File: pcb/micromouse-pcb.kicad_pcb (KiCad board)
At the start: 4 copper layers, 100 x 114 mm, 129 parts, among them J1 JST_XH_B2B-XH-A_1x02_P2.50mm_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, J10 PinSocket_1x08_P2.54mm_Vertic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, J11 PinSocket_1x08_P2.54mm_Vertic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, J2 PinHeader_1x02_P2.54mm_Vertic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, J3 JST_XH_B3B-XH-A_1x03_P2.50mm_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, J5 JST_PH_B6B-PH-K_1x06_P2.00mm_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, J6 JST_PH_B6B-PH-K_1x06_P2.00mm_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, Q1 SOT-23, Q10 LED_D3.0mm_Clear, Q11 SOT-23, Q12 LED_D3.0mm_Clear, Q13 SOT-23, Q14 SMD phototransistor 940nm, DA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, Q15 SOT-23, Q16 SMD phototransistor 940nm, DA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, Q17 SOT-23, Q18 SMD phototransistor 940nm, DA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, Q19 SOT-23, Q2 LED_D3.0mm_Clear, Q20 SMD phototransistor 940nm, DA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, Q21 SOT-23, Q22 SMD phototransistor 940nm, DA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, Q23 SOT-23, Q24 SMD phototransistor 940nm, DA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, Q25 SOT-23, Q26 SMD phototransistor 940nm, DA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, Q27 SOT-23, Q28 SMD phototransistor 940nm, DA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, Q29 SOT-23, Q3 SOT-23, Q30 SOT-23, Q31 SOT-23, Q32 SOT-23, Q33 SOT-23, Q34 SOT-23, Q35 SOT-23, Q36 SOT-23, Q37 SOT-23, Q4 LED_D3.0mm_Clear, Q5 SOT-23, Q6 LED_D3.0mm_Clear, Q7 SOT-23, Q8 LED_D3.0mm_Clear, Q9 SOT-23, SW1 SW_PUSH_6mm, U1 TSOT-23-6, U4 SOIC-24W_7.5x15.4mm_P1.27mm, U5 SOIC-24W_7.5x15.4mm_P1.27mm

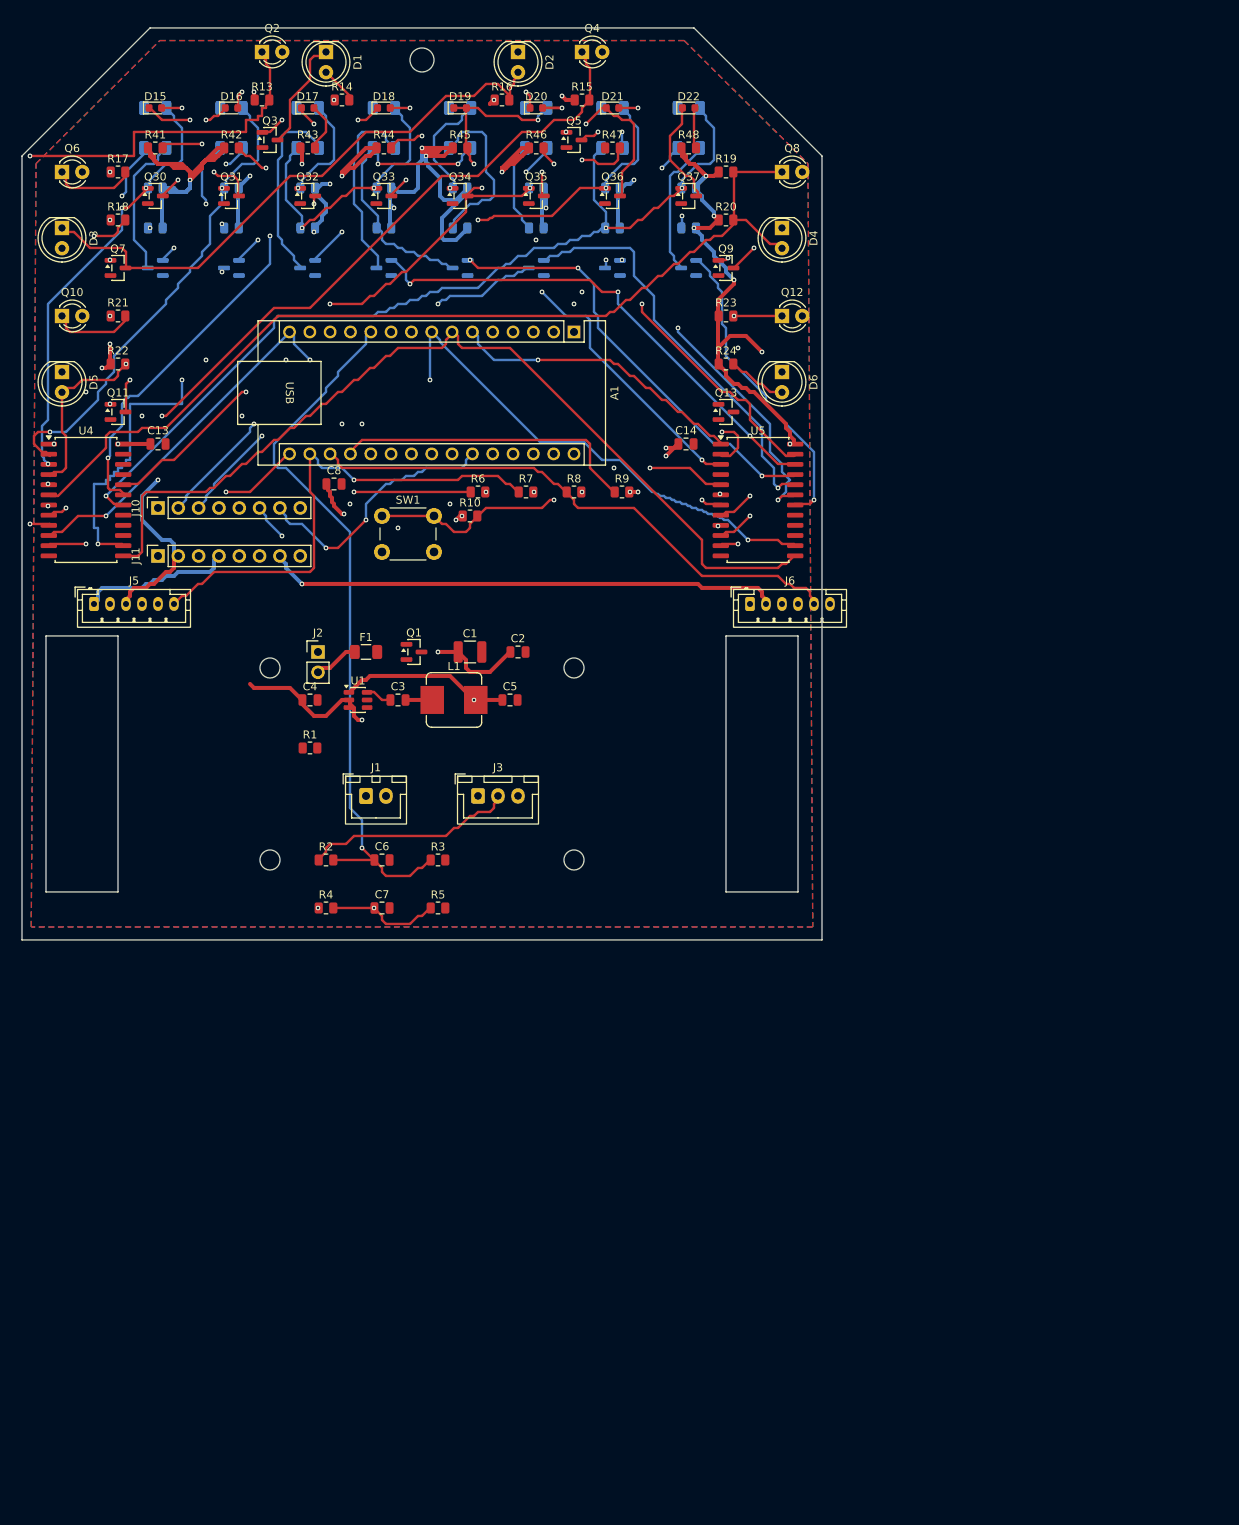
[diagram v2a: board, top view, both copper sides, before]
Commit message: Rev 4: WROOM-1 module, 1S power, direct wall ADC, pro routing
User requests: mux only for line array (walls direct to ADC), exact ESP32
library footprint+3D, exact N20 library, speed+RTOS, 1S LiPo, 3 user
buttons, rear USB-C, JTAG outlet, wall indicator LEDs, professional routing.

- ESP32-S3-WROOM-1 (SMD, stock footprint + 3D STEP), antenna overhanging
  the right edge per Espressif rules (interior placement disallowed).
  Locked pin map adversarially verified: JTAG on the real quad IO39-42,
  ENC2 on UART0 pins with 1k boot-contention guards (review blocker),
  straps as idle-low outputs with pull-downs, buttons IO0/35/36.
- 1S LiPo: TPS63001 buck-boost (buck can't hold 3.3V from a sagging cell),
  no balance lead, divider rescaled 4.2V->2.52V (ADC calibrated-range
  review fix), motors on raw cell (3V-wound N20s).
- Sensors: walls direct on ADC1 IO1-6 (fired pair sampled in parallel),
  line array on one CD74HC4067 (HC swap: HEF4067 out of spec at 3.3V),
  emitters ganged in 4 groups (U5 deleted), 6 PMOS wall indicators
  (LED ON = wall seen) + 8 line indicators on top.
- Project-local N20 library (footprint + hand-authored VRML from Pololu
  drawing 0J949); motors placed true-size, keep-outs match real 33mm body.
- Router upgrades: string-pulling post-pass (canonical diagonal+straight
  45-degree geometry, clearance-verified per candidate -- segment count
  halved), two power-width tiers (0.35mm for the SON-pad nets), padded
  slot/hole keep-outs, via-radius-aware keepout test.
- Fixed a real generator bug: loop Z-bend wires shorted nets every 6th
  sensor (netlist audit caught D3/D9 anodes folded into cathode nets) --
  all loop wiring is now straight by construction.

100x114mm, 4 layers, 152 footprints, 1077 tracks / 167 vias, ERC 0,
DRC 0 errors; 12 connections left for GUI finishing (JTAG fan-out, one
USB pair, buck-boost hookup) -- listed in PROJECT_NOTES.

Co-Authored-By: Claude Fable 5 <noreply@anthropic.com>
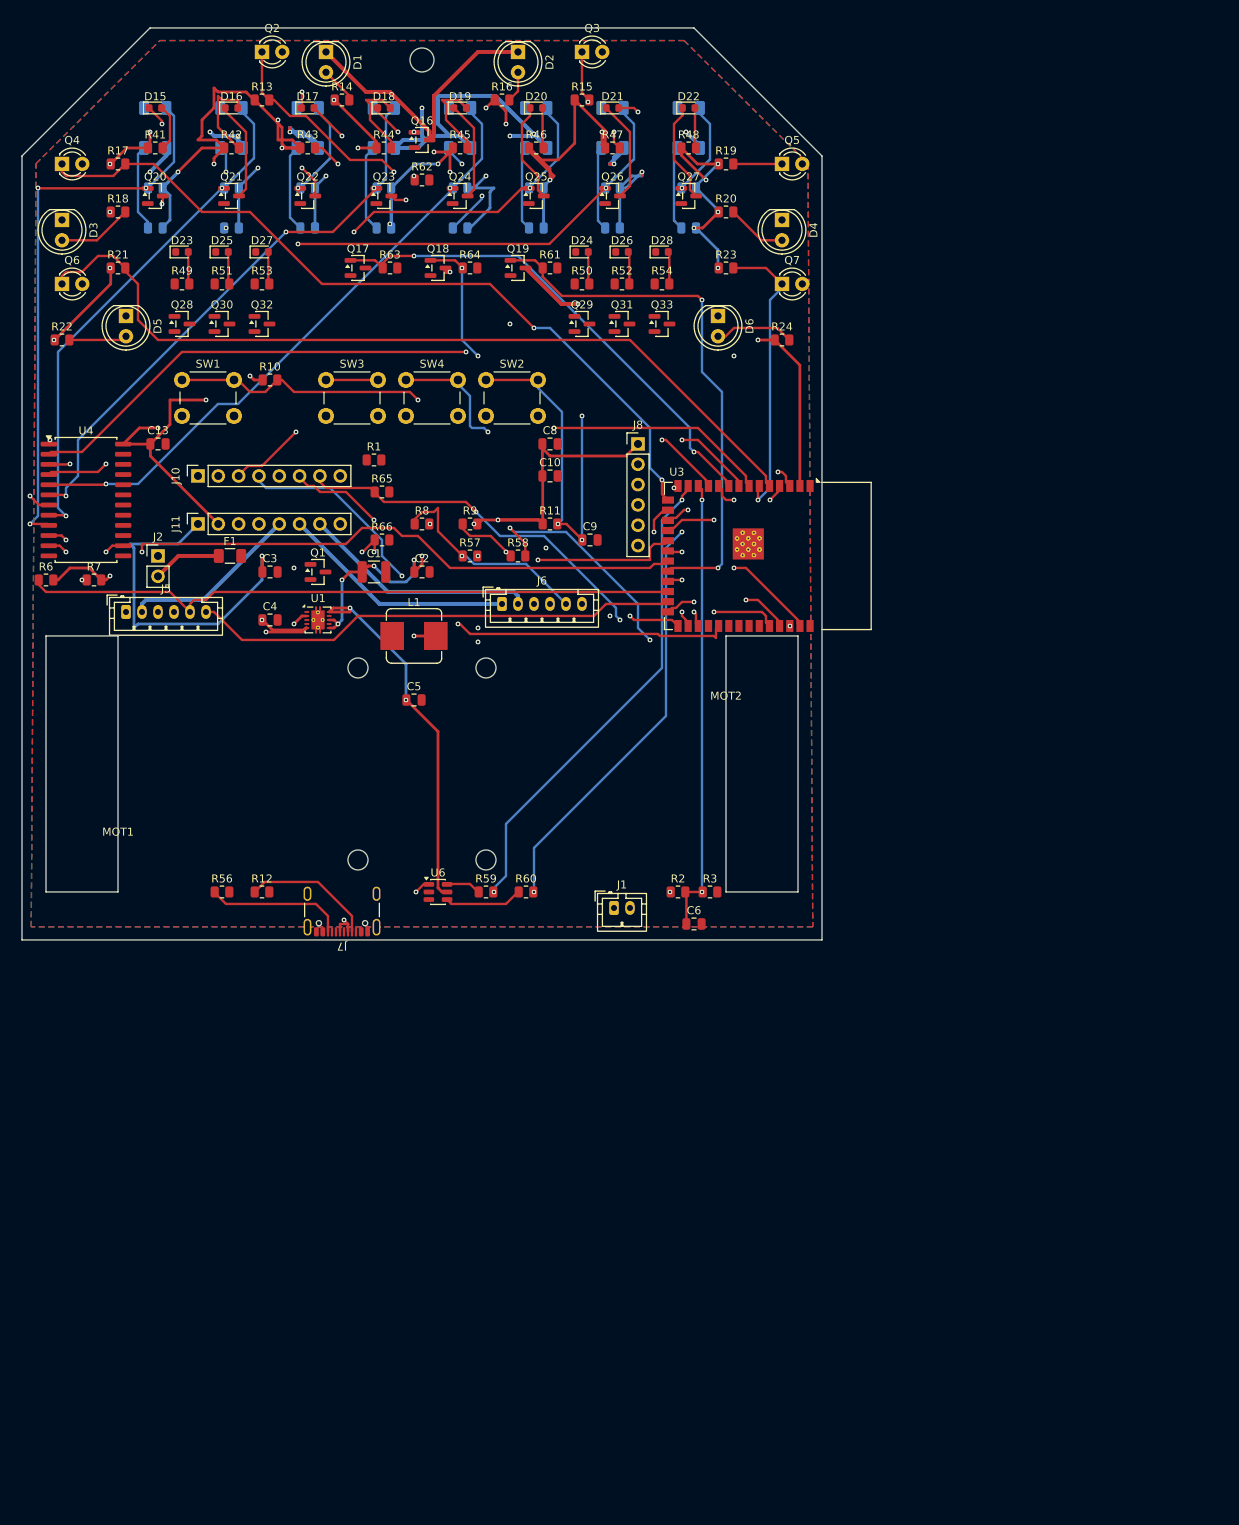
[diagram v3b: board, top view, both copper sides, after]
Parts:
- removed A1: Arduino_Nano, Arduino_Nano
- removed C14, C7: C_0805_2012Metric, C_0805_2012Metric
- removed J3: JST_XH_B3B-XH-A_1x03_P2.50mm_Vertical, JST_XH_B3B-XH-A_1x03_P2.50mm_Vertical
- removed Q34, Q35, Q36, Q37: SOT-23, SOT-23
- removed R4, R5: R_0805_2012Metric, R_0805_2012Metric
- removed U5: SOIC-24W_7.5x15.4mm_P1.27mm, SOIC-24W_7.5x15.4mm_P1.27mm
- added C10: C_0805_2012Metric, C_0805_2012Metric, F.Cu at (66.0, 56.0)
- added C9: C_0805_2012Metric, C_0805_2012Metric, F.Cu at (71.0, 64.0)
- added D23: LED_0603_1608Metric, LED_0603_1608Metric, F.Cu at (20.0, 28.0)
- added D24: LED_0603_1608Metric, LED_0603_1608Metric, F.Cu at (70.0, 28.0)
- added D25: LED_0603_1608Metric, LED_0603_1608Metric, F.Cu at (25.0, 28.0)
- added D26: LED_0603_1608Metric, LED_0603_1608Metric, F.Cu at (75.0, 28.0)
- added D27: LED_0603_1608Metric, LED_0603_1608Metric, F.Cu at (30.0, 28.0)
- added D28: LED_0603_1608Metric, LED_0603_1608Metric, F.Cu at (80.0, 28.0)
- added J7: USB_C_Receptacle_GCT_USB4105-xx-A_16P_TopMnt_Horizontal, USB_C_Receptacle_GCT_USB4105-xx-A_16P_TopMnt_Horizontal, F.Cu at (40.0, 109.3)
- added J8: PinHeader_1x06_P2.54mm_Vertical, PinHeader_1x06_P2.54mm_Vertical, F.Cu at (77.0, 52.0)
- added MOT1: N20_Motor_Encoder, N20_Motor_Encoder, F.Cu at (12.0, 92.0)
- added MOT2: N20_Motor_Encoder, N20_Motor_Encoder, F.Cu at (88.0, 92.0)
- added R11: R_0805_2012Metric, R_0805_2012Metric, F.Cu at (66.0, 62.0)
- added R12: R_0805_2012Metric, R_0805_2012Metric, F.Cu at (30.0, 108.0)
- added R49: R_0805_2012Metric, R_0805_2012Metric, F.Cu at (20.0, 32.0)
- added R50: R_0805_2012Metric, R_0805_2012Metric, F.Cu at (70.0, 32.0)
- added R51: R_0805_2012Metric, R_0805_2012Metric, F.Cu at (25.0, 32.0)
- added R52: R_0805_2012Metric, R_0805_2012Metric, F.Cu at (75.0, 32.0)
- added R53: R_0805_2012Metric, R_0805_2012Metric, F.Cu at (30.0, 32.0)
- added R54: R_0805_2012Metric, R_0805_2012Metric, F.Cu at (80.0, 32.0)
- added R56: R_0805_2012Metric, R_0805_2012Metric, F.Cu at (25.0, 108.0)
- added R57: R_0805_2012Metric, R_0805_2012Metric, F.Cu at (56.0, 66.0)
- added R58: R_0805_2012Metric, R_0805_2012Metric, F.Cu at (62.0, 66.0)
- added R59: R_0805_2012Metric, R_0805_2012Metric, F.Cu at (58.0, 108.0)
- added R60: R_0805_2012Metric, R_0805_2012Metric, F.Cu at (63.0, 108.0)
- added R61: R_0805_2012Metric, R_0805_2012Metric, F.Cu at (66.0, 30.0)
- added R62: R_0805_2012Metric, R_0805_2012Metric, F.Cu at (50.0, 19.0)
- added R63: R_0805_2012Metric, R_0805_2012Metric, F.Cu at (46.0, 30.0)
- added R64: R_0805_2012Metric, R_0805_2012Metric, F.Cu at (56.0, 30.0)
- added R65: R_0805_2012Metric, R_0805_2012Metric, F.Cu at (45.0, 58.0)
- added R66: R_0805_2012Metric, R_0805_2012Metric, F.Cu at (45.0, 64.0)
- added SW2: SW_PUSH_6mm, SW_PUSH_6mm, F.Cu at (58.0, 44.0)
- added SW3: SW_PUSH_6mm, SW_PUSH_6mm, F.Cu at (38.0, 44.0)
- added SW4: SW_PUSH_6mm, SW_PUSH_6mm, F.Cu at (48.0, 44.0)
- added U3: ESP32-S3-WROOM-1, ESP32-S3-WROOM-1, F.Cu at (93.2, 66.0)
- added U6: SOT-23-6, SOT-23-6, F.Cu at (52.0, 108.0)
- D15, D16, D17, D18, D19, D20, D21, D22: value Indicator LED 0603 super-red AlInGaP, high-efficiency bin REQUIRED at 1.4mA (e.g. Kingbright APT1608SURCK; LD271 base s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 -> LED_0603_1608Metric
- J1: value JST_XH_B2B-XH-A_1x02_P2.50mm_Vertical -> JST_PH_B2B-PH-K_1x02_P2.00mm_Vertical; footprint JST_XH_B2B-XH-A_1x02_P2.50mm_Vertical -> JST_PH_B2B-PH-K_1x02_P2.00mm_Vertical
- L1: value 3.3uH -> 1.5uH
- Q10, Q12, Q8: value LED_D3.0mm_Clear -> LED_1206_3216Metric; footprint LED_D3.0mm_Clear -> LED_1206_3216Metric; moved to B.Cu
- Q11, Q13, Q9: value SOT-23 -> LED_1206_3216Metric; footprint SOT-23 -> LED_1206_3216Metric; moved to B.Cu
- Q14: value SMD phototransistor 940nm, DAYLIGHT-FILTERED REQUIRED (e.g. Osram SFH320FA -- an unfiltered part re-opens optical feedb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 -> LED_1206_3216Metric
- Q15: value SOT-23 -> LED_1206_3216Metric; footprint SOT-23 -> LED_1206_3216Metric
- Q16, Q18, Q20, Q22, Q24, Q26, Q28: value SMD phototransistor 940nm, DAYLIGHT-FILTERED REQUIRED (e.g. Osram SFH320FA -- an unfiltered part re-opens optical feedb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 -> SOT-23; footprint LED_1206_3216Metric -> SOT-23; moved to F.Cu
- Q17, Q19, Q21, Q23, Q25, Q27, Q29: moved to F.Cu
- Q3, Q5, Q7: value SOT-23 -> LED_D3.0mm_Clear; footprint SOT-23 -> LED_D3.0mm_Clear
- R26, R28, R30, R32, R34, R36, R38, R40: value 120 -> R_0805_2012Metric
- U1: value TSOT-23-6 -> Texas_DRC0010J_ThermalVias; footprint TSOT-23-6 -> Texas_DRC0010J_ThermalVias
- moved Q7 83.0 mm to (95.0, 32.0)
- moved Q8 78.7 mm to (16.7, 10.0), turned to 180 degrees
- moved Q15 69.6 mm to (83.3, 10.0)
- moved Q28 68.9 mm to (20.0, 37.0), turned to 0 degrees
- moved Q4 66.5 mm to (5.00, 17.0)
- moved Q9 65.0 mm to (26.2, 10.0), turned to 180 degrees
- moved Q14 57.1 mm to (73.8, 10.0)
- moved R6 55.1 mm to (3.00, 69.0)
- moved R7 55.1 mm to (9.00, 69.0)
- moved Q31 51.4 mm to (75.0, 37.0)
- moved Q11 50.5 mm to (45.2, 10.0), turned to 180 degrees
- moved Q12 47.9 mm to (54.8, 10.0), turned to 180 degrees
- moved Q13 44.8 mm to (64.3, 10.0), turned to 180 degrees
- moved R2 44.2 mm to (82.0, 108.0)
- moved Q3 40.5 mm to (70.0, 3.00)
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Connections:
- net VBAT_CELL1_SENSE renamed VBAT_SENSE
- C3 pad 1: Net-(U1-BST) -> VM_BATT
- C3 pad 2: Net-(U1-SW) -> GND
- D1 pad 1: Net-(D1-K) -> EMIT_FRONT_K
- D10 pad 1: Net-(D10-K) -> EMIT_LINE_K
- D11 pad 1: Net-(D10-A) -> EMIT_LINE_K
- D12 pad 1: Net-(D12-K) -> EMIT_LINE_K
- D13 pad 1: Net-(D13-K) -> EMIT_LINE_K
- D13 pad 2: LINE8_SENSE -> Net-(D13-A)
- D14 pad 1: Net-(D14-K) -> EMIT_LINE_K
- D19 pad 1: LINE6_SENSE -> Net-(D19-K)
- D19 pad 2: LINE6_SENSE -> Net-(D19-A)
- D2 pad 1: Net-(D2-K) -> EMIT_FRONT_K
- D21 pad 1: Net-(D20-A) -> Net-(D21-K)
- D3 pad 1: Net-(D2-A) -> EMIT_DIAG_K
- D4 pad 1: Net-(D4-K) -> EMIT_DIAG_K
- D4 pad 2: WALL4_SENSE -> Net-(D4-A)
- D5 pad 1: Net-(D5-K) -> EMIT_SIDE_K
- D5 pad 2: WALL6_SENSE -> Net-(D5-A)
- D6 pad 1: Net-(D6-K) -> EMIT_SIDE_K
- D7 pad 1: Net-(D7-K) -> EMIT_LINE_K
- D8 pad 1: Net-(D8-K) -> EMIT_LINE_K
- D9 pad 1: Net-(D9-K) -> EMIT_LINE_K
- D9 pad 2: LINE4_SENSE -> Net-(D9-A)
- L1 pad 1: Net-(U1-SW) -> Net-(U1-L1)
- L1 pad 2: PLUS3V3 -> Net-(U1-L2)
- Q10 pad 1: WALL5_SENSE -> LINE3_SENSE
- Q11 pad 1: WALL5_LED -> LINE4_SENSE
- Q12 pad 1: WALL6_SENSE -> LINE5_SENSE
- Q13 pad 1: WALL6_LED -> LINE6_SENSE
- Q14 pad 1: LINE1_SENSE -> LINE7_SENSE
- Q15 pad 1: LINE1_LED -> LINE8_SENSE
- Q16 pad 1: LINE2_SENSE -> WALL_EMIT_FRONT
- Q17 pad 1: LINE2_LED -> WALL_EMIT_DIAG
- Q17 pad 3: Net-(D8-K) -> EMIT_DIAG_K
- Q18 pad 1: LINE3_SENSE -> WALL_EMIT_SIDE
- Q19 pad 1: LINE3_LED -> LINE_EMIT
- Q19 pad 3: Net-(D9-K) -> EMIT_LINE_K
- Q20 pad 1: LINE4_SENSE -> LINE1_SENSE
- Q21 pad 1: LINE4_LED -> LINE2_SENSE
- Q21 pad 3: Net-(D10-K) -> Net-(D16-K)
- Q22 pad 1: LINE5_SENSE -> LINE3_SENSE
- Q23 pad 1: LINE5_LED -> LINE4_SENSE
- Q23 pad 3: Net-(D10-A) -> Net-(D18-K)
- Q24 pad 1: LINE6_SENSE -> LINE5_SENSE
- Q25 pad 1: LINE6_LED -> LINE6_SENSE
- Q25 pad 3: Net-(D12-K) -> Net-(D20-K)
- Q27 pad 1: LINE7_LED -> LINE8_SENSE
- Q27 pad 3: Net-(D13-K) -> Net-(D22-K)
- Q28 pad 1: LINE8_SENSE -> (no net)
- Q28 pad 2: GND -> (no net)
- Q29 pad 1: LINE8_LED -> (no net)
- Q29 pad 2: GND -> (no net)
- Q29 pad 3: Net-(D14-K) -> (no net)
- Q3 pad 1: WALL1_LED -> WALL2_SENSE
- Q30 pad 1: LINE1_SENSE -> (no net)
- Q30 pad 2: GND -> (no net)
- Q30 pad 3: Net-(D15-K) -> (no net)
- Q31 pad 1: LINE2_SENSE -> (no net)
- Q31 pad 2: GND -> (no net)
- Q31 pad 3: Net-(D16-K) -> (no net)
- Q32 pad 1: LINE3_SENSE -> (no net)
- Q32 pad 2: GND -> (no net)
- Q32 pad 3: Net-(D17-K) -> (no net)
- Q33 pad 1: LINE4_SENSE -> (no net)
- Q33 pad 2: GND -> (no net)
- Q33 pad 3: Net-(D18-K) -> (no net)
- Q4 pad 1: WALL2_SENSE -> WALL3_SENSE
- Q5 pad 1: WALL2_LED -> WALL4_SENSE
- Q6 pad 1: WALL3_SENSE -> WALL5_SENSE
- Q7 pad 1: WALL3_LED -> WALL6_SENSE
- Q8 pad 1: WALL4_SENSE -> LINE1_SENSE
- Q9 pad 1: WALL4_LED -> LINE2_SENSE
- R2 pad 1: Net-(J3-Pin_2) -> VM_BATT
- R20 pad 2: WALL4_SENSE -> Net-(D4-A)
- R22 pad 2: WALL6_SENSE -> Net-(D5-A)
- R30 pad 2: LINE4_SENSE -> Net-(D9-A)
- R38 pad 2: LINE8_SENSE -> Net-(D13-A)
- R45 pad 2: LINE6_SENSE -> Net-(D19-A)
- U1 pad 2: VM_BATT -> Net-(U1-L2)
- U1 pad 3: VM_BATT -> GND
- U1 pad 4: GND -> Net-(U1-L1)
- U1 pad 5: Net-(U1-SW) -> VM_BATT
- U1 pad 6: Net-(U1-BST) -> VM_BATT
- U4 pad 13: MUX_S3 -> GND
- U4 pad 18: LINE8_SENSE -> unconnected-(U4-I13-Pad18)
- U4 pad 19: LINE7_SENSE -> unconnected-(U4-I12-Pad19)
- U4 pad 2: LINE2_SENSE -> LINE8_SENSE
- U4 pad 20: LINE6_SENSE -> unconnected-(U4-I11-Pad20)
- U4 pad 21: LINE5_SENSE -> unconnected-(U4-I10-Pad21)
- U4 pad 22: LINE4_SENSE -> unconnected-(U4-I9-Pad22)
- U4 pad 23: LINE3_SENSE -> unconnected-(U4-I8-Pad23)
- U4 pad 3: LINE1_SENSE -> LINE7_SENSE
- U4 pad 4: WALL6_SENSE -> LINE6_SENSE
- U4 pad 5: WALL5_SENSE -> LINE5_SENSE
- U4 pad 6: WALL4_SENSE -> LINE4_SENSE
- U4 pad 7: WALL3_SENSE -> LINE3_SENSE
- U4 pad 8: WALL2_SENSE -> LINE2_SENSE
- U4 pad 9: WALL1_SENSE -> LINE1_SENSE
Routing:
- net EMIT_LINE_K: track 0.00 -> 180.8 mm, vias 0 -> 10
- net MUX_S3: track 116.0 -> 0.00 mm
- net VBAT_PACK_SENSE: track 99.1 -> 0.00 mm, vias 1 -> 0
- net WALL3_LED: track 94.4 -> 0.00 mm, vias 3 -> 0
- net WALL1_LED: track 91.4 -> 0.00 mm, vias 3 -> 0
- net VM_BATT: track 65.9 -> 154.8 mm, vias 2 -> 9
- net LINE1_LED: track 84.1 -> 0.00 mm, vias 3 -> 0
- net EMIT_SIDE_K: track 0.00 -> 81.2 mm, vias 0 -> 2
- net WALL5_LED: track 80.9 -> 0.00 mm, vias 3 -> 0
- net LINE2_LED: track 78.0 -> 0.00 mm, vias 3 -> 0
- net ESP_EN: track 0.00 -> 75.6 mm, vias 0 -> 4
- net LINE3_LED: track 75.2 -> 0.00 mm, vias 2 -> 0
- net WALL5_SENSE: track 33.9 -> 105.7 mm, vias 1 -> 0
- net Net-(D2-A): track 74.1 -> 3.91 mm
- net WALL4_SENSE: track 121.1 -> 51.0 mm, vias 0 -> 1
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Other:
- outline, holes or cut-outs redrawn
